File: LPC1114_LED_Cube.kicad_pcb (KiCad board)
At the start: 2 copper layers, 100 x 100 mm, 88 parts, among them Q201 BSS138, Q202 BSS138, Q203 BSS138, Q204 BSS138, Q205 IRLML6402TRPBF, Q206 IRLML6402TRPBF, Q207 IRLML6402TRPBF, Q208 IRLML6402TRPBF, Q209 BSS138, Q210 BSS138, Q211 BSS138, Q212 BSS138, Q213 IRLML6402TRPBF, Q214 IRLML6402TRPBF, Q215 IRLML6402TRPBF, Q216 IRLML6402TRPBF, Y101 12MHZ, Y102 12MHZ

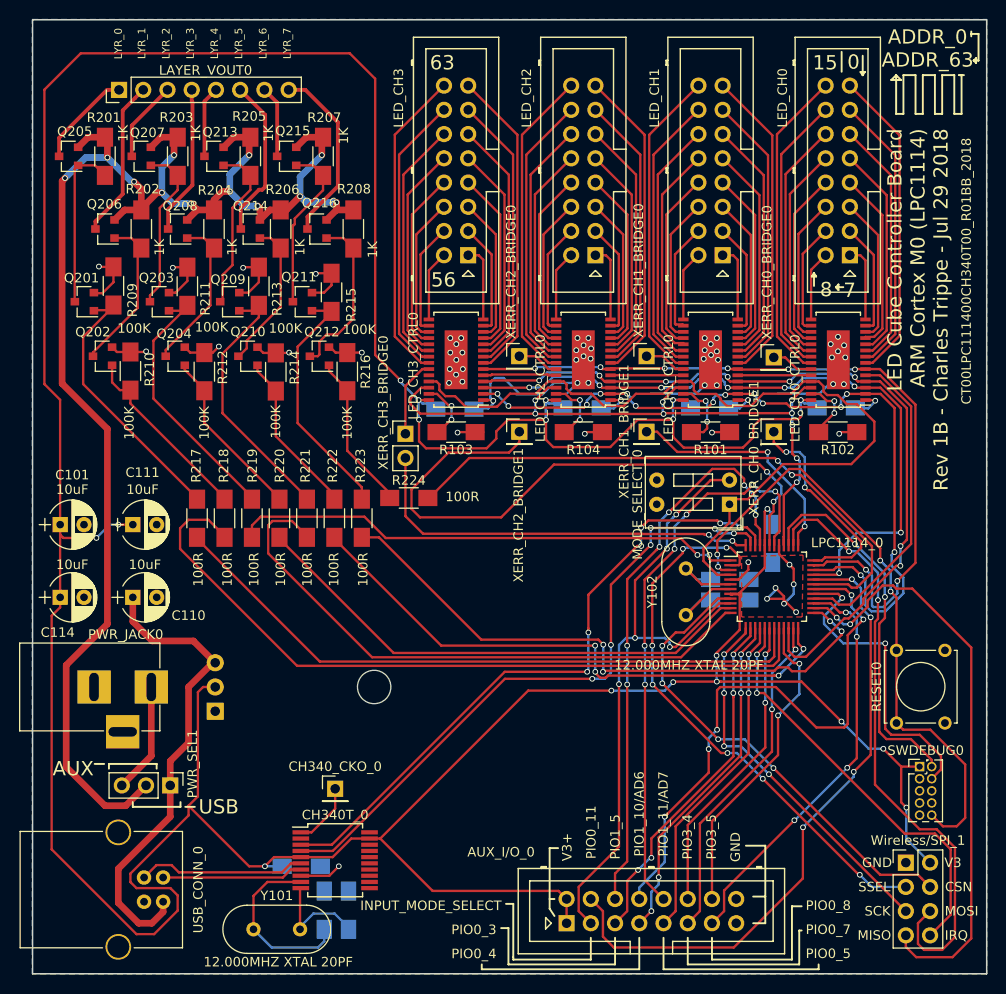
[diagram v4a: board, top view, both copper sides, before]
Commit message: changed some pinouts Added hardware flow control lines between MCU and serial IC
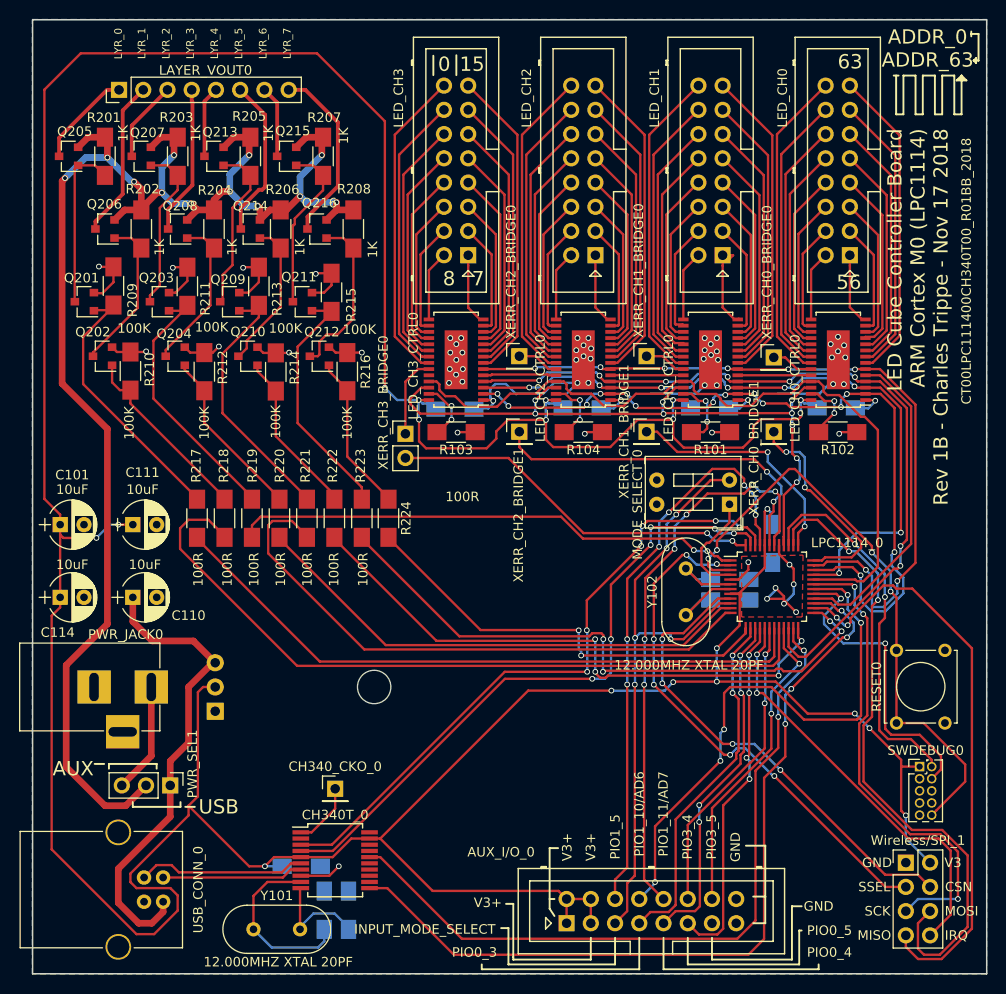
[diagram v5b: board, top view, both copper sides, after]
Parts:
- R209, R210, R211, R212, R213, R214, R215, R216: value 1K -> 100K
- moved R224 3.01 mm to (122.3, 97.2), turned to 270 degrees
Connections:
- net SOUT renamed Net-(LED_CH3_CTRL0-Pad24)
- AUX_I/O_0 pad 11: PIO0_7 -> PIO0_5
- AUX_I/O_0 pad 13: PIO0_8 -> GND
- AUX_I/O_0 pad 3: INPUT_MODE_SELECT -> V3
- AUX_I/O_0 pad 4: PIO0_11 -> V3
- AUX_I/O_0 pad 5: PIO0_3 -> INPUT_MODE_SELECT
- AUX_I/O_0 pad 7: PIO0_4 -> PIO0_3
- AUX_I/O_0 pad 9: PIO0_5 -> PIO0_4
- CH340T_0 pad 11: Net-(CH340T_0-Pad11) -> _RTS_MCU
- CH340T_0 pad 16: Net-(CH340T_0-Pad16) -> _CTS_MCU
- LED_CH0_CTRL0 pad 25: ISP_ENTRY -> LED_GS_CLK
- LED_CH1_CTRL0 pad 25: ISP_ENTRY -> LED_GS_CLK
- LED_CH2_CTRL0 pad 25: ISP_ENTRY -> LED_GS_CLK
- LED_CH3_CTRL0 pad 25: ISP_ENTRY -> LED_GS_CLK
- LPC1114_0 pad 13: AUX_SPI_SCK -> LAYER_7_ON
- LPC1114_0 pad 23: PIO0_7 -> _CTS_MCU
- LPC1114_0 pad 27: PIO0_8 -> _RTS_MCU
- LPC1114_0 pad 31: LAYER_7_ON -> AUX_SPI_SCK
- LPC1114_0 pad 32: PIO0_11 -> LED_GS_CLK
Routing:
- net _RTS_MCU: track 0.00 -> 87.3 mm, vias 0 -> 4
- net LED_GS_CLK: track 0.00 -> 80.9 mm
- net _CTS_MCU: track 0.00 -> 78.2 mm, vias 0 -> 2
- net ISP_ENTRY: track 88.8 -> 12.0 mm
- net PIO0_11: track 68.1 -> 0.00 mm, vias 4 -> 0
- net PIO0_8: track 43.4 -> 0.00 mm, vias 4 -> 0
- net PIO0_7: track 35.7 -> 0.00 mm, vias 2 -> 0
- net XERR_MCU_CH2: track 65.5 -> 37.5 mm
- net LAYER_7_ON: track 61.8 -> 45.9 mm
- net AUX_SPI_SCK: track 39.6 -> 50.2 mm, vias 4 -> 3
- net V3: track 437.0 -> 441.8 mm
- net AUX_SPI_MOSI: track 64.7 -> 68.5 mm
- net XERR_MCU_CH3: track 43.0 -> 39.4 mm
- net AUX_SPI_SSEL: track 59.1 -> 56.1 mm, vias 7 -> 6
- net INPUT_MODE_SELECT: track 67.8 -> 64.8 mm
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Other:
- board text added: "LED Cube Controller Board ARM Cortex M0 (LPC1114) Rev 1B - Charles Trippe - Nov 17 2018"
- board text removed: "LED Cube Controller Board ARM Cortex M0 (LPC1114) Rev 1B - Charles Trippe - Jul 29 2018"
- board text removed: "PIO0_11"
- board text removed: "PIO0_7"
- board text removed: "PIO0_8"
